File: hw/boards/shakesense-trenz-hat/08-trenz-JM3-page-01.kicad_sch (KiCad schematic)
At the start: 1 part, among them J82 LSHM-130-04.0-L-DV-A-S-K-TR

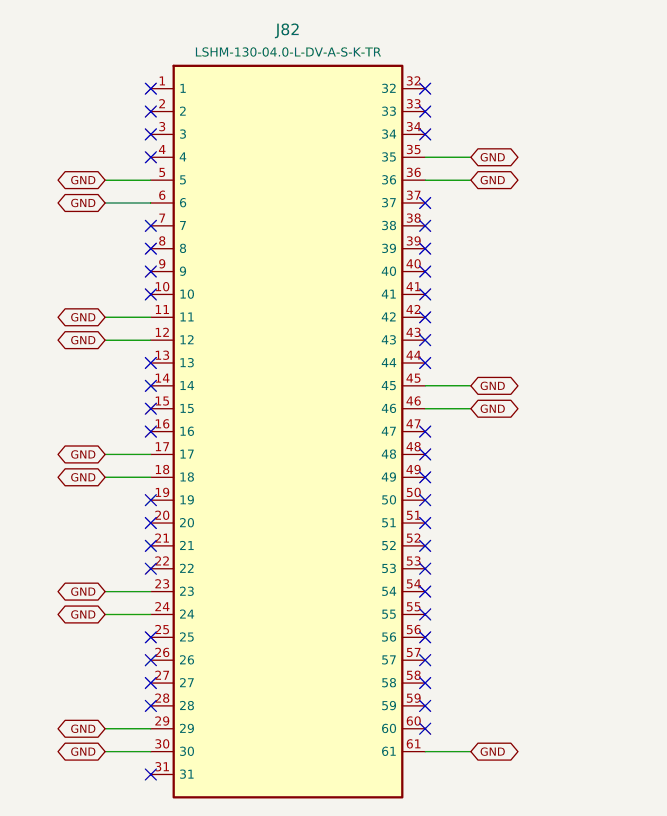
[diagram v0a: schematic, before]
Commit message: Expose Trenz GPIOs on the Pi-outline HDI sensor HAT
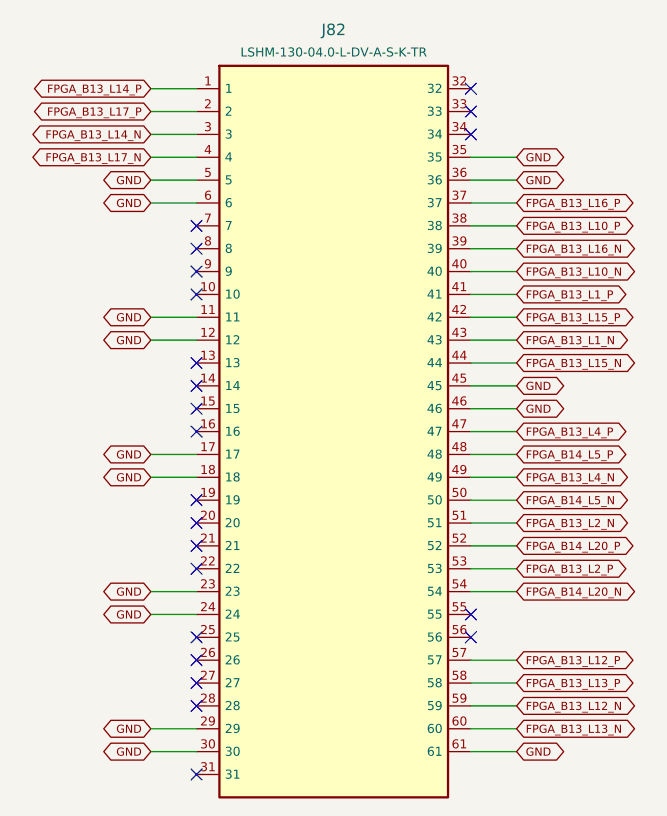
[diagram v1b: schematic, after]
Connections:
- net FPGA_B13_L14_P: now reaches J82.1
- net FPGA_B13_L17_P: now reaches J82.2
- net FPGA_B13_L14_N: now reaches J82.3
- net FPGA_B13_L16_P: now reaches J82.37
- net FPGA_B13_L10_P: now reaches J82.38
- net FPGA_B13_L16_N: now reaches J82.39
- net FPGA_B13_L17_N: now reaches J82.4
- net FPGA_B13_L10_N: now reaches J82.40
- net FPGA_B13_L1_P: now reaches J82.41
- net FPGA_B13_L15_P: now reaches J82.42
- net FPGA_B13_L1_N: now reaches J82.43
- net FPGA_B13_L15_N: now reaches J82.44
- net FPGA_B13_L4_P: now reaches J82.47
- net FPGA_B14_L5_P: now reaches J82.48
- net FPGA_B13_L4_N: now reaches J82.49
- net FPGA_B14_L5_N: now reaches J82.50
- net FPGA_B13_L2_N: now reaches J82.51
- net FPGA_B14_L20_P: now reaches J82.52
- net FPGA_B13_L2_P: now reaches J82.53
- net FPGA_B14_L20_N: now reaches J82.54
- net FPGA_B13_L12_P: now reaches J82.57
- net FPGA_B13_L13_P: now reaches J82.58
- net FPGA_B13_L12_N: now reaches J82.59
- net FPGA_B13_L13_N: now reaches J82.60
- no-connect marks 46 -> 22
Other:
- title: shakesense-trenz-hat / 08-trenz-JM3-page-01 -> ShakeSense T1 / 08-trenz-JM3-page-01
- moved on the sheet: J82

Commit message: Implement internal Pi FPGA link and remove ribbon expansion
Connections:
- net FPGA_B13_L10_N: no longer names the net of J82.40
- net FPGA_B13_L10_P: no longer names the net of J82.38
- net FPGA_B13_L12_N: no longer names the net of J82.59
- net FPGA_B13_L12_P: no longer names the net of J82.57
- net FPGA_B13_L13_N: no longer names the net of J82.60
- net FPGA_B13_L13_P: no longer names the net of J82.58
- net FPGA_B13_L14_N: no longer names the net of J82.3
- net FPGA_B13_L14_P: no longer names the net of J82.1
- net FPGA_B13_L15_N: no longer names the net of J82.44
- net FPGA_B13_L15_P: no longer names the net of J82.42
- net FPGA_B13_L16_N: no longer names the net of J82.39
- net FPGA_B13_L16_P: no longer names the net of J82.37
- net FPGA_B13_L17_N: no longer names the net of J82.4
- net FPGA_B13_L17_P: no longer names the net of J82.2
- net FPGA_B13_L1_N: no longer names the net of J82.43
- net FPGA_B13_L1_P: no longer names the net of J82.41
- net FPGA_B13_L2_N: no longer names the net of J82.51
- net FPGA_B13_L2_P: no longer names the net of J82.53
- net FPGA_B13_L4_N: no longer names the net of J82.49
- net FPGA_B13_L4_P: no longer names the net of J82.47
- net FPGA_B14_L20_N: no longer names the net of J82.54
- net FPGA_B14_L20_P: no longer names the net of J82.52
- net FPGA_B14_L5_N: no longer names the net of J82.50
- net FPGA_B14_L5_P: no longer names the net of J82.48
- no-connect marks 22 -> 46
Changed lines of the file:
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@@
               (property "MPN" "LSHM-130-04.0-L-DV-A-S-K-TR" (at 50.8 76.2 0) (effects (font (size 1 1)) hide))
               (instances (project "shakesense-trenz-hat" (path "/4ffaaa5d-c728-540d-9f0f-f1cafbdbe36e/67714a77-f600-51cc-abba-303e92e2b0df" (reference "J82") (unit 1)))))
-(wire (pts (xy 35.56 38.1) (xy 30.48 38.1)) (stroke (width 0) (type default)))
-(global_label "FPGA_B13_L14_P" (shape bidirectional) (at 30.48 38.1 180) (effects (font (size 0.9 0.9)) (justify right)))
-(wire (pts (xy 35.56 40.64) (xy 30.48 40.64)) (stroke (width 0) (type default)))
-(global_label "FPGA_B13_L17_P" (shape bidirectional) (at 30.48 40.64 180) (effects (font (size 0.9 0.9)) (justify right)))
-(wire (pts (xy 35.56 43.18) (xy 30.48 43.18)) (stroke (width 0) (type default)))
-(global_label "FPGA_B13_L14_N" (shape bidirectional) (at 30.48 43.18 180) (effects (font (size 0.9 0.9)) (justify right)))
-(wire (pts (xy 35.56 45.72) (xy 30.48 45.72)) (stroke (width 0) (type default)))
-(global_label "FPGA_B13_L17_N" (shape bidirectional) (at 30.48 45.72 180) (effects (font (size 0.9 0.9)) (justify right)))
+(no_connect (at 35.56 38.1))
+(no_connect (at 35.56 40.64))
+(no_connect (at 35.56 43.18))
+(no_connect (at 35.56 45.72))
 (wire (pts (xy 35.56 48.26) (xy 30.48 48.26)) (stroke (width 0) (type default)))
 (global_label "GND" (shape bidirectional) (at 30.48 48.26 180) (effects (font (size 0.9 0.9)) (justify right)))
@@
 (wire (pts (xy 66.04 48.26) (xy 71.12 48.26)) (stroke (width 0) (type default)))
 (global_label "GND" (shape bidirectional) (at 71.12 48.26 0) (effects (font (size 0.9 0.9)) (justify left)))
-(wire (pts (xy 66.04 50.8) (xy 71.12 50.8)) (stroke (width 0) (type default)))
-(global_label "FPGA_B13_L16_P" (shape bidirectional) (at 71.12 50.8 0) (effects (font (size 0.9 0.9)) (justify left)))
-(wire (pts (xy 66.04 53.34) (xy 71.12 53.34)) (stroke (width 0) (type default)))
-(global_label "FPGA_B13_L10_P" (shape bidirectional) (at 71.12 53.34 0) (effects (font (size 0.9 0.9)) (justify left)))
-(wire (pts (xy 66.04 55.88) (xy 71.12 55.88)) (stroke (width 0) (type default)))
-(global_label "FPGA_B13_L16_N" (shape bidirectional) (at 71.12 55.88 0) (effects (font (size 0.9 0.9)) (justify left)))
-(wire (pts (xy 66.04 58.42) (xy 71.12 58.42)) (stroke (width 0) (type default)))
-(global_label "FPGA_B13_L10_N" (shape bidirectional) (at 71.12 58.42 0) (effects (font (size 0.9 0.9)) (justify left)))
-(wire (pts (xy 66.04 60.96) (xy 71.12 60.96)) (stroke (width 0) (type default)))
-(global_label "FPGA_B13_L1_P" (shape bidirectional) (at 71.12 60.96 0) (effects (font (size 0.9 0.9)) (justify left)))
-(wire (pts (xy 66.04 63.5) (xy 71.12 63.5)) (stroke (width 0) (type default)))
-(global_label "FPGA_B13_L15_P" (shape bidirectional) (at 71.12 63.5 0) (effects (font (size 0.9 0.9)) (justify left)))
-(wire (pts (xy 66.04 66.04) (xy 71.12 66.04)) (stroke (width 0) (type default)))
-(global_label "FPGA_B13_L1_N" (shape bidirectional) (at 71.12 66.04 0) (effects (font (size 0.9 0.9)) (justify left)))
-(wire (pts (xy 66.04 68.58) (xy 71.12 68.58)) (stroke (width 0) (type default)))
-(global_label "FPGA_B13_L15_N" (shape bidirectional) (at 71.12 68.58 0) (effects (font (size 0.9 0.9)) (justify left)))
+(no_connect (at 66.04 50.8))
+(no_connect (at 66.04 53.34))
+(no_connect (at 66.04 55.88))
+(no_connect (at 66.04 58.42))
+(no_connect (at 66.04 60.96))
+(no_connect (at 66.04 63.5))
+(no_connect (at 66.04 66.04))
+(no_connect (at 66.04 68.58))
 (wire (pts (xy 66.04 71.12) (xy 71.12 71.12)) (stroke (width 0) (type default)))
 (global_label "GND" (shape bidirectional) (at 71.12 71.12 0) (effects (font (size 0.9 0.9)) (justify left)))
 (wire (pts (xy 66.04 73.66) (xy 71.12 73.66)) (stroke (width 0) (type default)))
 (global_label "GND" (shape bidirectional) (at 71.12 73.66 0) (effects (font (size 0.9 0.9)) (justify left)))
-(wire (pts (xy 66.04 76.2) (xy 71.12 76.2)) (stroke (width 0) (type default)))
-(global_label "FPGA_B13_L4_P" (shape bidirectional) (at 71.12 76.2 0) (effects (font (size 0.9 0.9)) (justify left)))
-(wire (pts (xy 66.04 78.74) (xy 71.12 78.74)) (stroke (width 0) (type default)))
-(global_label "FPGA_B14_L5_P" (shape bidirectional) (at 71.12 78.74 0) (effects (font (size 0.9 0.9)) (justify left)))
-(wire (pts (xy 66.04 81.28) (xy 71.12 81.28)) (stroke (width 0) (type default)))
-(global_label "FPGA_B13_L4_N" (shape bidirectional) (at 71.12 81.28 0) (effects (font (size 0.9 0.9)) (justify left)))
-(wire (pts (xy 66.04 83.82) (xy 71.12 83.82)) (stroke (width 0) (type default)))
-(global_label "FPGA_B14_L5_N" (shape bidirectional) (at 71.12 83.82 0) (effects (font (size 0.9 0.9)) (justify left)))
-(wire (pts (xy 66.04 86.36) (xy 71.12 86.36)) (stroke (width 0) (type default)))
-(global_label "FPGA_B13_L2_N" (shape bidirectional) (at 71.12 86.36 0) (effects (font (size 0.9 0.9)) (justify left)))
-(wire (pts (xy 66.04 88.9) (xy 71.12 88.9)) (stroke (width 0) (type default)))
-(global_label "FPGA_B14_L20_P" (shape bidirectional) (at 71.12 88.9 0) (effects (font (size 0.9 0.9)) (justify left)))
-(wire (pts (xy 66.04 91.44) (xy 71.12 91.44)) (stroke (width 0) (type default)))
-(global_label "FPGA_B13_L2_P" (shape bidirectional) (at 71.12 91.44 0) (effects (font (size 0.9 0.9)) (justify left)))
-(wire (pts (xy 66.04 93.98) (xy 71.12 93.98)) (stroke (width 0) (type default)))
-(global_label "FPGA_B14_L20_N" (shape bidirectional) (at 71.12 93.98 0) (effects (font (size 0.9 0.9)) (justify left)))
+(no_connect (at 66.04 76.2))
+(no_connect (at 66.04 78.74))
+(no_connect (at 66.04 81.28))
+(no_connect (at 66.04 83.82))
+(no_connect (at 66.04 86.36))
+(no_connect (at 66.04 88.9))
+(no_connect (at 66.04 91.44))
+(no_connect (at 66.04 93.98))
 (no_connect (at 66.04 96.52))
 (no_connect (at 66.04 99.06))
-(wire (pts (xy 66.04 101.6) (xy 71.12 101.6)) (stroke (width 0) (type default)))
-(global_label "FPGA_B13_L12_P" (shape bidirectional) (at 71.12 101.6 0) (effects (font (size 0.9 0.9)) (justify left)))
-(wire (pts (xy 66.04 104.14) (xy 71.12 104.14)) (stroke (width 0) (type default)))
-(global_label "FPGA_B13_L13_P" (shape bidirectional) (at 71.12 104.14 0) (effects (font (size 0.9 0.9)) (justify left)))
-(wire (pts (xy 66.04 106.68) (xy 71.12 106.68)) (stroke (width 0) (type default)))
-(global_label "FPGA_B13_L12_N" (shape bidirectional) (at 71.12 106.68 0) (effects (font (size 0.9 0.9)) (justify left)))
-(wire (pts (xy 66.04 109.22) (xy 71.12 109.22)) (stroke (width 0) (type default)))
-(global_label "FPGA_B13_L13_N" (shape bidirectional) (at 71.12 109.22 0) (effects (font (size 0.9 0.9)) (justify left)))
+(no_connect (at 66.04 101.6))
+(no_connect (at 66.04 104.14))
+(no_connect (at 66.04 106.68))
+(no_connect (at 66.04 109.22))
 (wire (pts (xy 66.04 111.76) (xy 71.12 111.76)) (stroke (width 0) (type default)))
 (global_label "GND" (shape bidirectional) (at 71.12 111.76 0) (effects (font (size 0.9 0.9)) (justify left)))
